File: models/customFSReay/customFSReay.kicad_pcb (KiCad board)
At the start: 2 copper layers, 126 x 43 mm, 10 parts

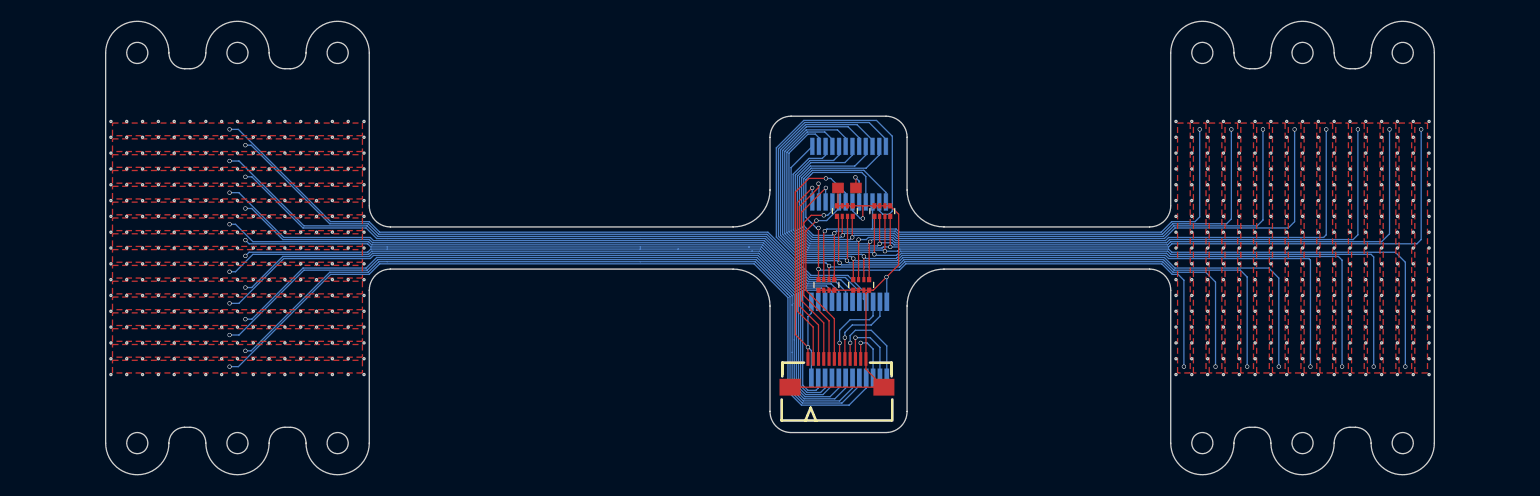
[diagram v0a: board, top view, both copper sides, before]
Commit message: modify the fixation position to fit better on finger
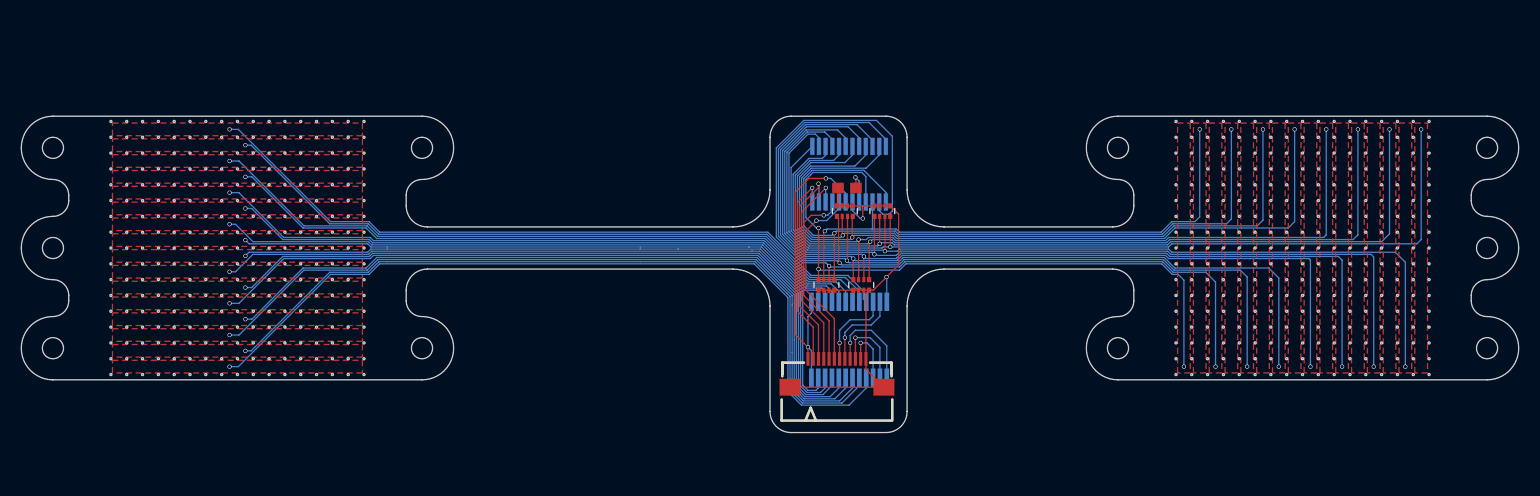
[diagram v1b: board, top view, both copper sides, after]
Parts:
- moved G*** 2.50 mm to (108.2, 110.8)
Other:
- board size 126 x 43 mm -> 142 x 30 mm
- board text added: "By adev & cqz"
- board text removed: "By adev &"

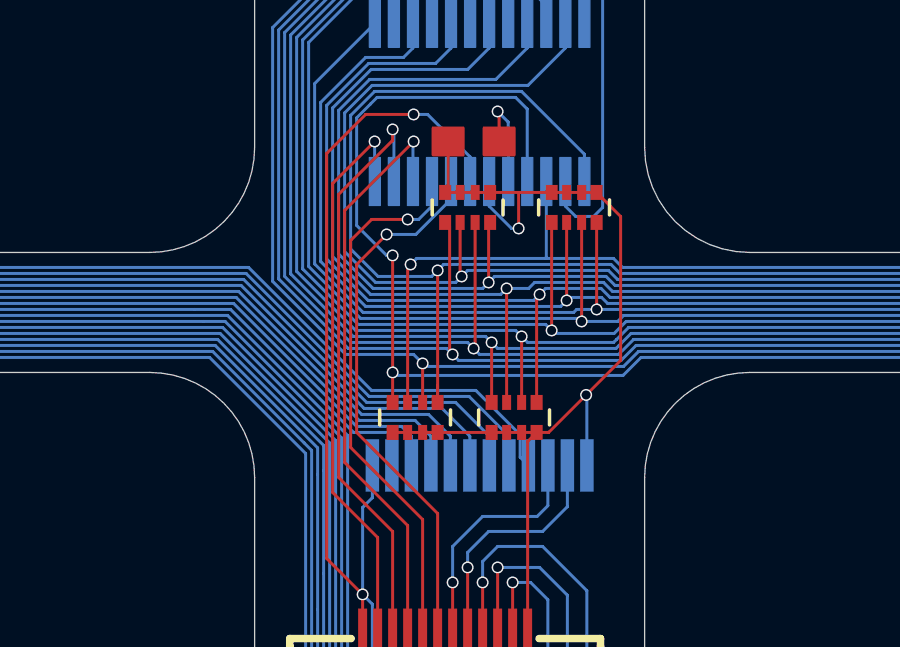
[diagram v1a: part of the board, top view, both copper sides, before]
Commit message: added teeardrops
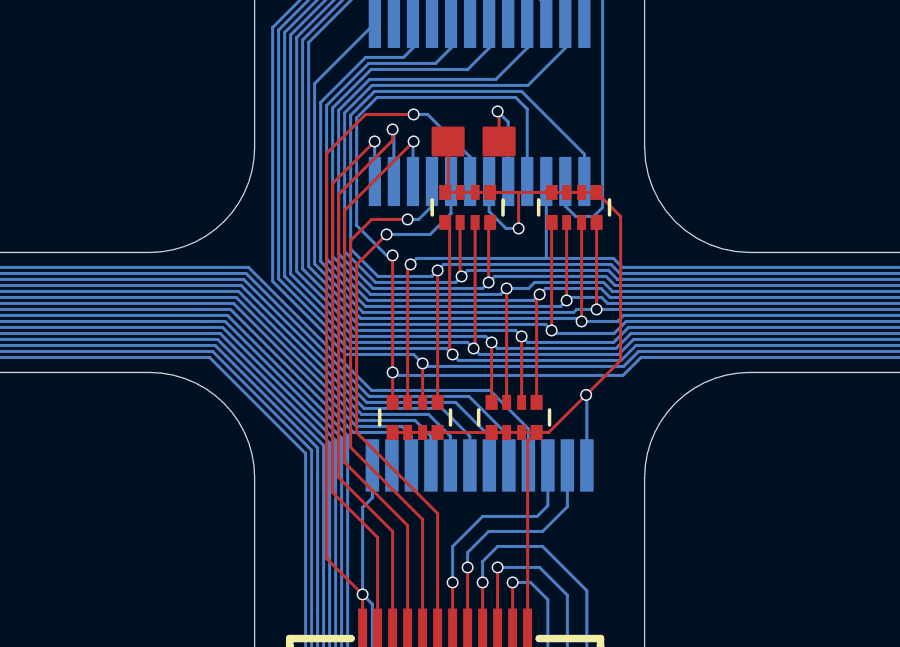
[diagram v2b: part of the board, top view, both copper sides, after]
